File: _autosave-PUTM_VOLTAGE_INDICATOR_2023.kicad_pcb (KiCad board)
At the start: 2 copper layers, 42.4 x 61.1 mm, 41 parts, among them IC1 LM211DT, J1 HV+, J2 HV-, Q1 TK3P80E,RQ, U1 LT8316EFE

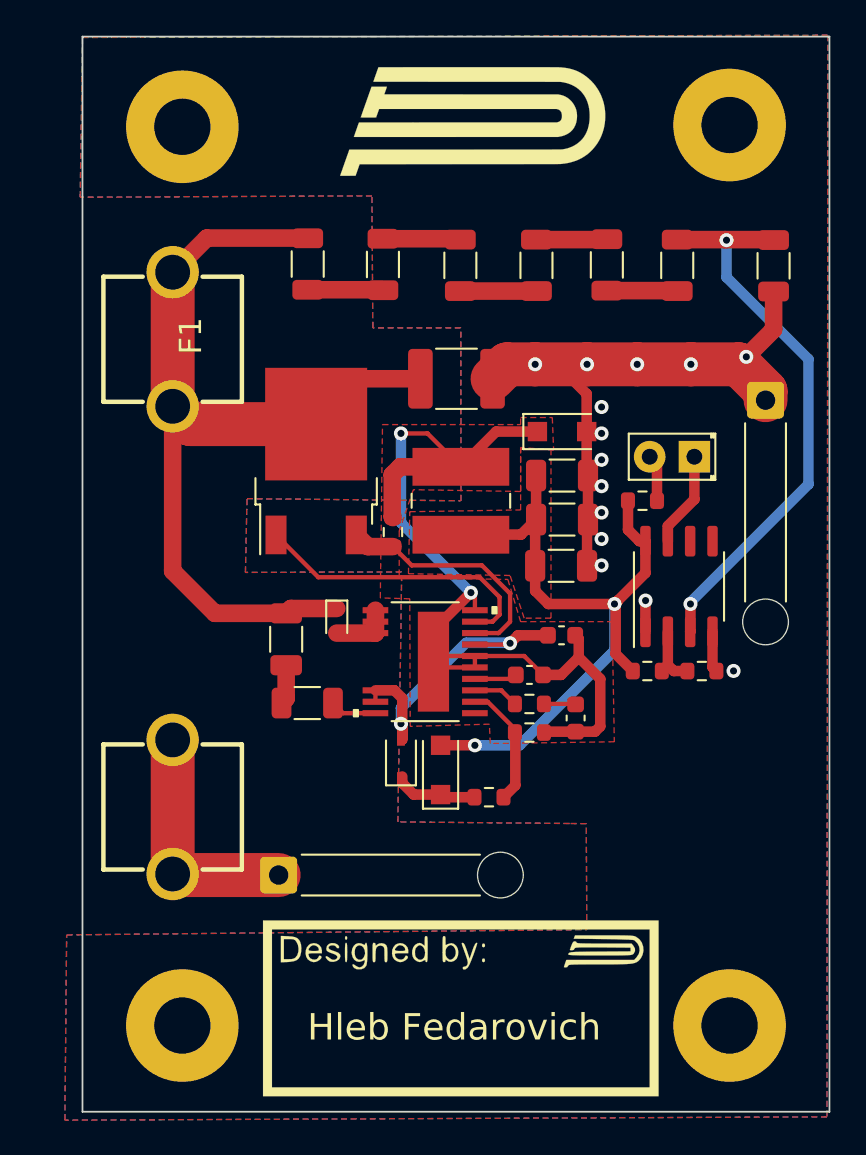
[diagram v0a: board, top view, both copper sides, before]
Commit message: fuse position changed/ small pcb updates
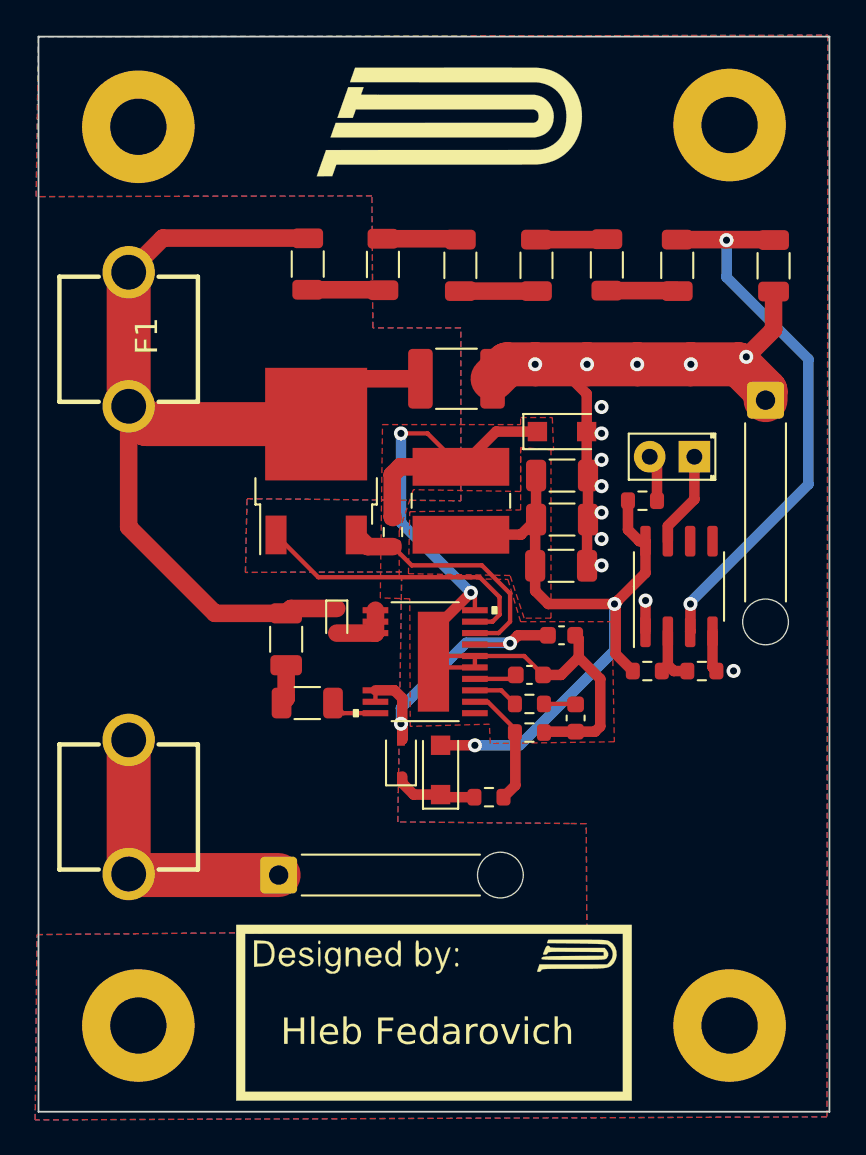
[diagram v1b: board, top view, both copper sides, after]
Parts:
- moved F1 2.50 mm to (95.1, 102.2)
- moved G*** 1.54 mm to (113.7, 140.4)
- moved G*** 1.33 mm to (112.9, 89.6)
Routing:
- net +VDC: track 51.5 -> 57.5 mm
- net Net-(F1-Pad2): track 13.7 -> 16.2 mm
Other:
- board size 42.4 x 61.1 mm -> 44.9 x 61.1 mm
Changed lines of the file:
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@@
   )
   (footprint "SignatureBox25mm" (layer "F.Cu")
-    (at 115.248833 140.175)
+    (at 113.725 140.425)
     (attr through_hole)
     (fp_text reference "G***" (at 0 0) (layer "F.SilkS") hide
@@
   )
   (footprint "PUTM_LOGO_18mm" (layer "F.Cu")
-    (at 114.215874 89.609565)
+    (at 112.890874 89.634565)
     (attr through_hole)
     (fp_text reference "G***" (at 0 0) (layer "F.SilkS") hide
@@
       (effects (font (size 1.27 1.27) (thickness 0.15)))
     )
-    (pad "1" thru_hole circle (at 0.35 0) (size 6.4 6.4) (drill 3.2) (layers *.Cu *.Mask))
+    (pad "1" thru_hole circle (at -2.15 0) (size 6.4 6.4) (drill 3.2) (layers *.Cu *.Mask))
   )
   (footprint "Connector_Wire:SolderWire-0.5sqmm_1x01_D0.9mm_OD2.1mm_Relief" (layer "F.Cu")
@@
       (effects (font (size 1.27 1.27) (thickness 0.15)))
     )
-    (pad "1" thru_hole circle (at -0.825 -0.7) (size 6.4 6.4) (drill 3.2) (layers *.Cu *.Mask))
+    (pad "1" thru_hole circle (at -3.325 -0.7) (size 6.4 6.4) (drill 3.2) (layers *.Cu *.Mask))
   )
   (footprint "vindicator:01020071Z-FUSE-CLIP" (layer "F.Cu")
-    (at 97.625 102.15 -90)
+    (at 95.125 102.15 -90)
     (descr "01020071Z-Fuse-Clip")
     (tags "Connector")
@@
     )
   )
-  (gr_rect (start 92.5 84.95) (end 134.95 146.05) (layer "Edge.Cuts") (width 0.1) (fill none))
+  (gr_rect (start 90 84.95) (end 134.95 146.05) (layer "Edge.Cuts") (width 0.1) (fill none))
   (segment (start 117.250502 118.975) (end 118.95 118.975) (width 0.6) (layer "F.Cu") (net 1))
   (segment (start 110.675 124.075) (end 110.675 124.9) (width 0.6) (layer "F.Cu") (net 1))
@@
   (segment (start 116.899998 121.450002) (end 117.125 121.225) (width 0.25) (layer "F.Cu") (net 4))
   (segment (start 114.800001 121.450002) (end 116.899998 121.450002) (width 0.25) (layer "F.Cu") (net 4))
+  (segment (start 95.125 98.34) (end 95.125 105.96) (width 2.5) (layer "F.Cu") (net 5))
   (segment (start 104.35 117.45) (end 104.075 117.725) (width 1) (layer "F.Cu") (net 5))
+  (segment (start 105.779 106.971) (end 96.136 106.971) (width 2.5) (layer "F.Cu") (net 5))
+  (segment (start 100.025 117.725) (end 95.125 112.825) (width 1) (layer "F.Cu") (net 5))
+  (segment (start 106.95 117.45) (end 104.35 117.45) (width 1) (layer "F.Cu") (net 5))
+  (segment (start 105.3 96.4125) (end 105.2875 96.4) (width 1) (layer "F.Cu") (net 5))
+  (segment (start 111.704 104.396) (end 108.354 104.396) (width 1) (layer "F.Cu") (net 5))
+  (segment (start 95.125 112.825) (end 95.125 105.96) (width 1) (layer "F.Cu") (net 5))
+  (segment (start 97.065 96.4) (end 95.125 98.34) (width 1) (layer "F.Cu") (net 5))
+  (segment (start 108.354 104.396) (end 105.779 106.971) (width 1) (layer "F.Cu") (net 5))
+  (segment (start 96.136 106.971) (end 95.125 105.96) (width 2.5) (layer "F.Cu") (net 5))
   (segment (start 104.075 117.725) (end 100.025 117.725) (width 1) (layer "F.Cu") (net 5))
-  (segment (start 106.95 117.45) (end 104.35 117.45) (width 1) (layer "F.Cu") (net 5))
-  (segment (start 99.565 96.4) (end 105.2875 96.4) (width 1) (layer "F.Cu") (net 5))
-  (segment (start 97.625 98.34) (end 99.565 96.4) (width 1) (layer "F.Cu") (net 5))
-  (segment (start 105.779 106.971) (end 98.636 106.971) (width 2.5) (layer "F.Cu") (net 5))
-  (segment (start 111.704 104.396) (end 108.354 104.396) (width 1) (layer "F.Cu") (net 5))
-  (segment (start 98.636 106.971) (end 97.625 105.96) (width 2.5) (layer "F.Cu") (net 5))
-  (segment (start 97.625 98.34) (end 97.625 105.96) (width 2.5) (layer "F.Cu") (net 5))
-  (segment (start 108.354 104.396) (end 105.779 106.971) (width 1) (layer "F.Cu") (net 5))
-  (segment (start 100.025 117.725) (end 97.625 115.325) (width 1) (layer "F.Cu") (net 5))
-  (segment (start 105.2875 96.4) (end 105.3 96.4125) (width 1) (layer "F.Cu") (net 5))
-  (segment (start 97.625 115.325) (end 97.625 105.96) (width 1) (layer "F.Cu") (net 5))
+  (segment (start 105.2875 96.4) (end 97.065 96.4) (width 1) (layer "F.Cu") (net 5))
   (segment (start 119.4 103.9) (end 116.3 103.9) (width 0.6) (layer "F.Cu") (net 6))
   (segment (start 131.318 105.6132) (end 131.318 105.093) (width 2.5) (layer "F.Cu") (net 6))
@@
   (segment (start 106.95 118.85) (end 109.149999 118.849999) (width 1) (layer "F.Cu") (net 12))
   (segment (start 109.149999 117.55) (end 109.149999 118.200001) (width 1) (layer "F.Cu") (net 12))
-  (segment (start 97.625 124.92) (end 97.625 132.54) (width 2.5) (layer "F.Cu") (net 13))
-  (segment (start 103.65 132.6) (end 97.685 132.6) (width 2.5) (layer "F.Cu") (net 13))
-  (segment (start 97.685 132.6) (end 97.625 132.54) (width 2.5) (layer "F.Cu") (net 13))
+  (segment (start 95.185 132.6) (end 95.125 132.54) (width 2.5) (layer "F.Cu") (net 13))
+  (segment (start 95.125 124.92) (end 95.125 132.54) (width 2.5) (layer "F.Cu") (net 13))
+  (segment (start 103.65 132.6) (end 95.185 132.6) (width 2.5) (layer "F.Cu") (net 13))
   (segment (start 129.1 96.52) (end 129.07 96.52) (width 0.6) (layer "F.Cu") (net 14))
   (segment (start 131.75 96.4875) (end 131.775 96.5125) (width 1) (layer "F.Cu") (net 14))
@@
     (connect_pads yes (clearance 0.508))
     (min_thickness 0.254) (filled_areas_thickness no)
-    (fill yes (thermal_gap 0.508) (thermal_bridge_width 0.508))
+    (fill (thermal_gap 0.508) (thermal_bridge_width 0.508))
     (polygon
       (pts
         (xy 134.86 84.87)
         (xy 134.81 146.34)
-        (xy 91.5 146.53)
-        (xy 91.6 136)
+        (xy 89.812642 146.513977)
+        (xy 89.912642 135.983977)
         (xy 121.16 135.7)
         (xy 121.13 129.68)
@@
         (xy 109 101.5)
         (xy 108.95 94)
-        (xy 92.37 94.08)
-        (xy 92.5 85)
+        (xy 89.866878 94.044163)
+        (xy 89.996878 84.964163)
       )
     )
@@
     (connect_pads yes (clearance 0.508))
     (min_thickness 0.254) (filled_areas_thickness no)
-    (fill yes (thermal_gap 0.508) (thermal_bridge_width 0.508))
+    (fill (thermal_gap 0.508) (thermal_bridge_width 0.508))
     (polygon
       (pts
@@
     (connect_pads yes (clearance 0.508))
     (min_thickness 0.254) (filled_areas_thickness no)
-    (fill yes (thermal_gap 0.508) (thermal_bridge_width 0.508))
+    (fill (thermal_gap 0.508) (thermal_bridge_width 0.508))
     (polygon
       (pts
